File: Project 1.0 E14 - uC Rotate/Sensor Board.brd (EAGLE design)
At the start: 40 x 75 mm, 97 parts, among them IC1 LT1963EST-1.5, IC2 LT1963EST-1.5, IC3 LT1963EST-1.5, IC4 LT1963EST-1.5, X1 87438-02, X3 87438-04

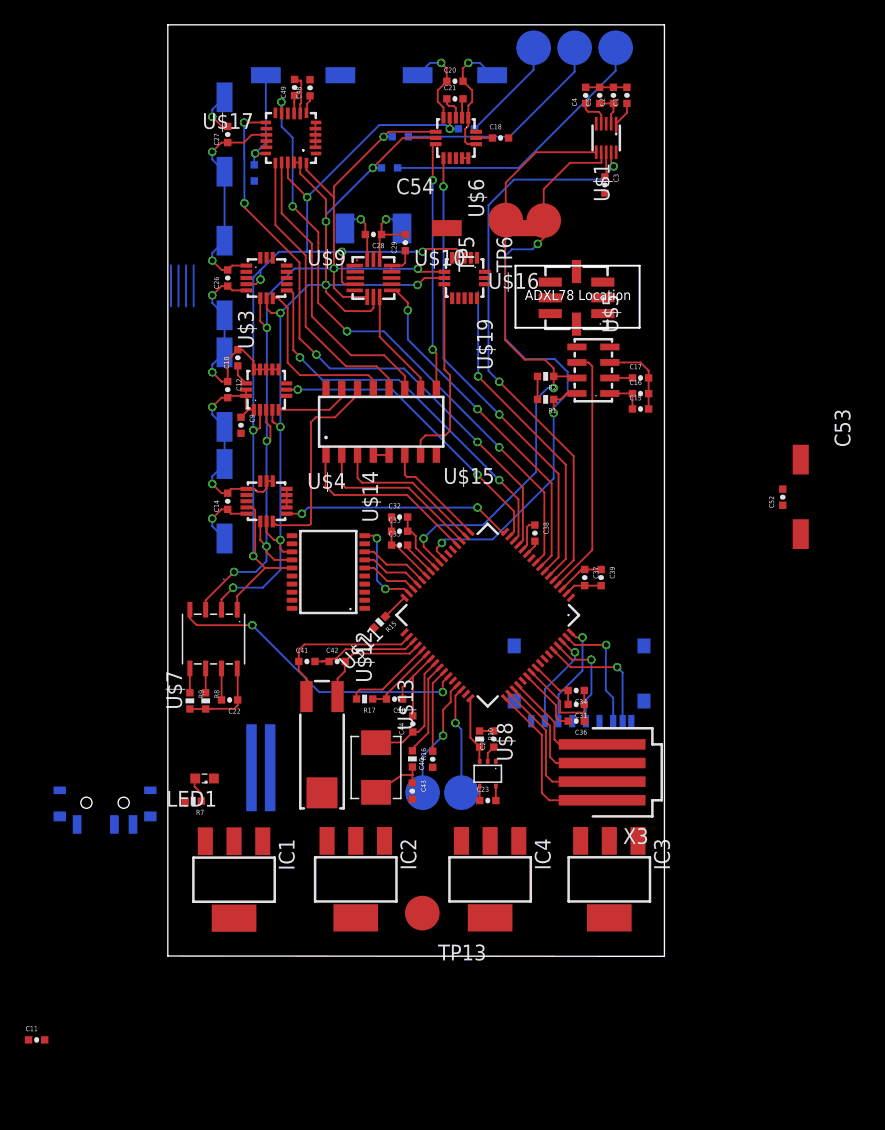
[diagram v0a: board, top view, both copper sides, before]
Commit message: Added H3LIS331 to library, Added H3LIS331 to schematic and removed ADXL78
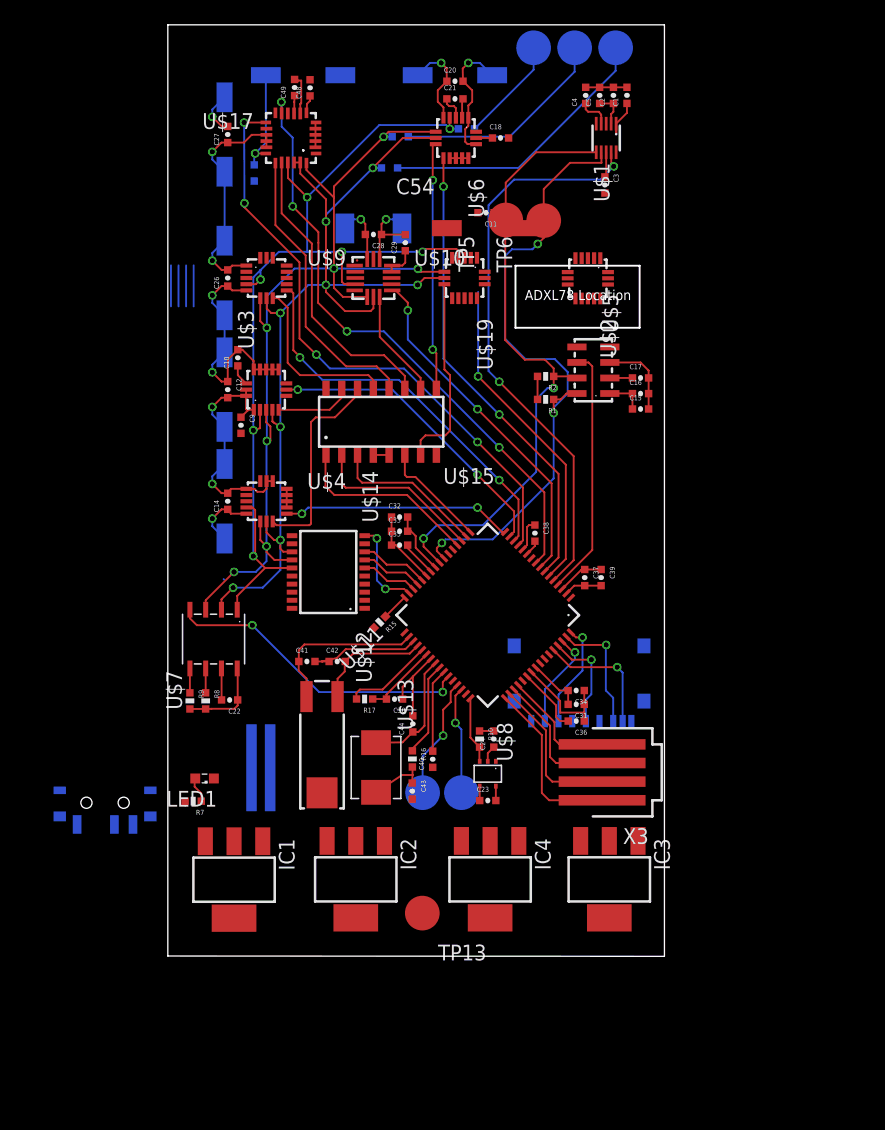
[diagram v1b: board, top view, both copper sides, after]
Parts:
- removed C52: 0.1uF, Kas-Passives:0402-CAP
- removed C53: 4.7uF, Kas-Passives:4.3X7.3SMD
- removed U$16: ADXL78, Kas-Sensors:LCC-8(5X5)_HS
- added U$2: H3LIS331DLTR_HS, Kas-Sensors:LGA-16(3X3)_HS
- moved C11 75.8 mm to (25.6, 59.9), turned to 180 degrees
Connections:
- removed net ADXL78-ST: U$16.P$4
- new net CS-H3LIS331DLTR: U$2.P$8
- new net N$37: U$2.P$1
- new net N$38: U$2.P$16
- new net N$39: U$2.P$14
- net 5.0V: no longer C52.1, C53.P$1, U$16.P$7, U$16.P$8
- net ANALOG-OUT-ADXL78: no longer U$16.P$6
- net GND: now also U$2.P$12, U$2.P$13, U$2.P$5; no longer C52.2, C53.P$2, U$16.P$3
- net MISO-B: now also U$2.P$7
- net MOSI-B: now also U$2.P$6
- net SCLK-B: now also U$2.P$4
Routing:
- net GND: track 92.5 -> 93.5 mm

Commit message: Sensor Board: Changed connector footprints to the correct model. Removed ADXL78 and replaced with H3LIS331DLTR.
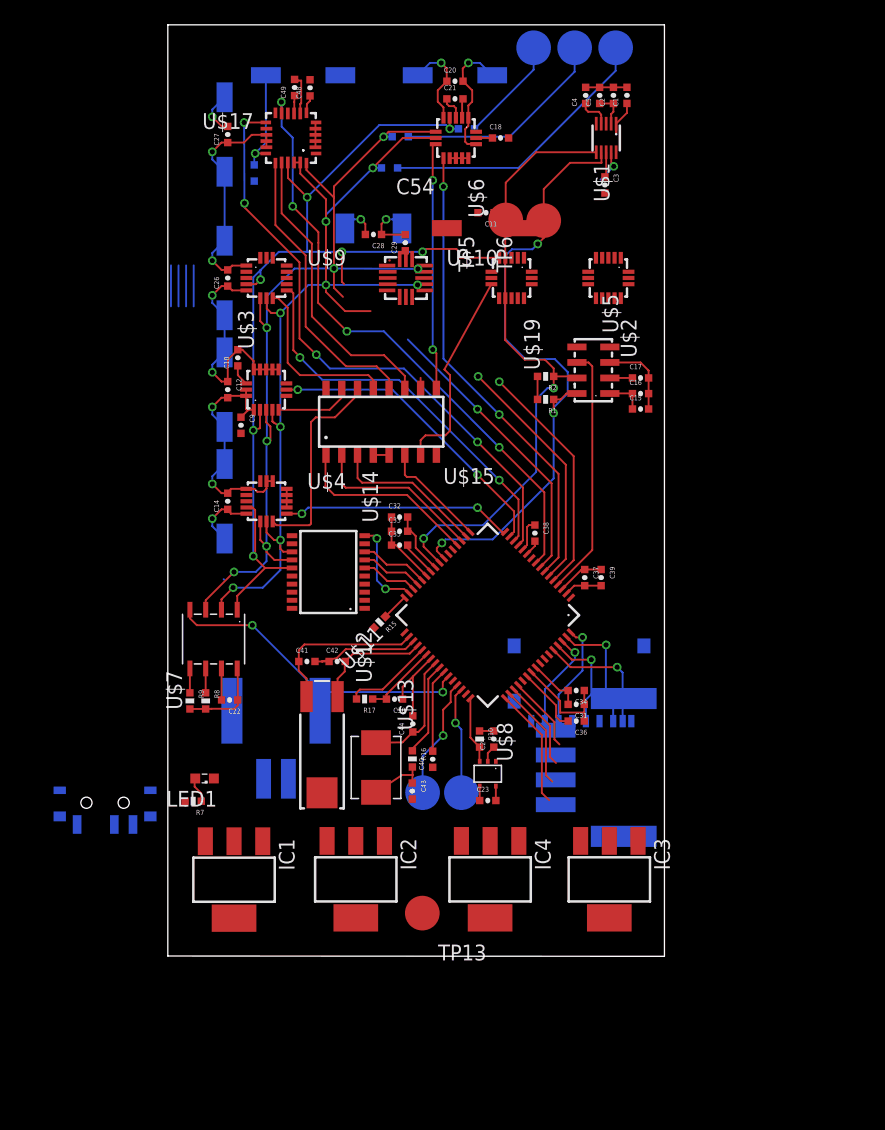
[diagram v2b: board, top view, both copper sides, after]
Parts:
- removed X1: 87438-02, con-molex:87438-02
- removed X3: 87438-04, con-molex:87438-04
- added U$16: 5023520200, Kas-Connectors:5023520200
- added U$20: 5023520410, Kas-Connectors:5023520410
- moved U$19 3.78 mm to (27.7, 54.6)
- moved U$10 2.62 mm to (19.2, 54.6)
- moved U$2 1.65 mm to (35.5, 54.6)
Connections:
- net GND: now also U$16.P$1; no longer X1.1
- net N$19: now also U$16.P$2; no longer X1.2
- net SWCLK: now also U$20.P$1; no longer X3.4
- net SWDIO: now also U$20.P$2; no longer X3.3
- net SWO: now also U$20.P$4; no longer X3.1
- net TDI: now also U$20.P$3; no longer X3.2
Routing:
- net INT1-MAG3110: track 46.4 -> 22.0 mm
- net CS-ADXL362: track 8.75 -> 0.86 mm
- net INT2-MAX21000: track 26.3 -> 19.5 mm
- net MOSI-B: track 80.2 -> 75.5 mm
- net INT2-ADXL362: track 28.1 -> 23.5 mm, vias 2 -> 1
- net SWO: track 14.0 -> 9.68 mm
- net TDI: track 12.5 -> 8.49 mm
- net SWDIO: track 11.0 -> 7.33 mm
- net MISO-B: track 79.3 -> 75.7 mm
- net GND: track 93.5 -> 90.0 mm
- net SWCLK: track 9.58 -> 6.15 mm
- net SCLK-B: track 84.1 -> 87.0 mm
- net 3.3V: track 96.7 -> 94.9 mm
- net CS-MAX21000: track 15.9 -> 16.8 mm
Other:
- outline, holes or cut-outs redrawn
- board text removed: "ADXL78 Location"
- board text removed: "FIX Footprint"
- board text removed: "H3LIS331DLTR should be used instead of teh ADXL78"

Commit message: Sensor Board: Removed all errors in PCB layout and most errors in schematic view. This was mainly achived by removing traces on the PCB and adding node names on the schematic
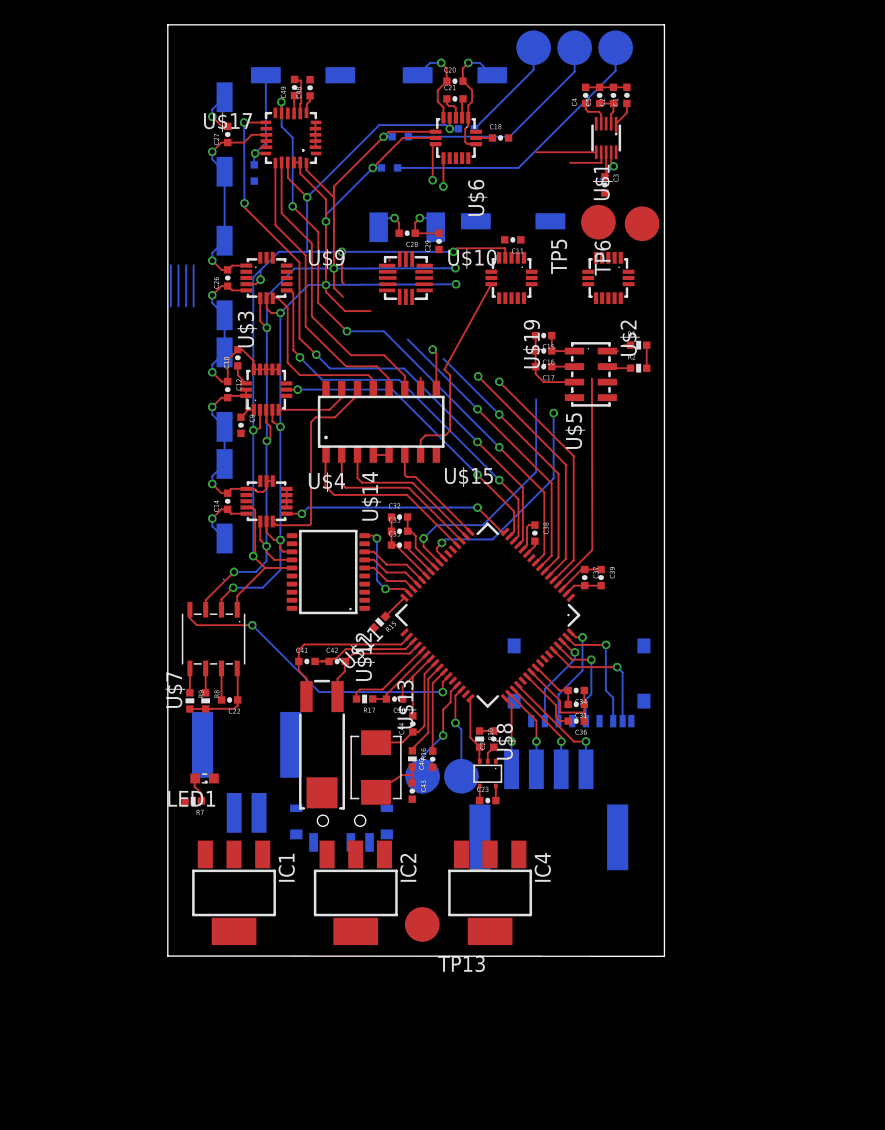
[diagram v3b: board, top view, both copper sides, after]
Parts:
- removed IC3: LT1963EST-1.5, linear-technology:SOT223
- C11: value CAPACITOR -> NO VALUE
- C54: value (none) -> NO VALUE
- U$19: value (none) -> MAX21000_HS
- moved S1 19.1 mm to (14.0, 10.9)
- moved U$20 12.0 mm to (30.7, 6.91), turned to 0 degrees
- moved C15 9.79 mm to (30.3, 50.0), turned to 180 degrees
- moved R1 8.67 mm to (37.9, 49.2), turned to 0 degrees
- moved C16 8.52 mm to (30.3, 48.7), turned to 180 degrees
- moved TP6 7.93 mm to (38.2, 59.0)
- moved C17 7.85 mm to (30.3, 47.5), turned to 180 degrees
- moved R2 7.52 mm to (37.9, 47.3), turned to 0 degrees
- moved TP5 7.47 mm to (34.7, 59.1)
- moved U$16 3.62 mm to (6.35, 19.7)
- moved C11 3.07 mm to (27.8, 57.7)
- moved C19 2.72 mm to (19.3, 58.7)
- moved C28 2.72 mm to (19.3, 58.2)
- moved C29 2.72 mm to (21.8, 57.6)
- moved C54 2.40 mm to (27.8, 59.2), flipped to the bottom, turned to 0 degrees
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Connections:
- removed net 5.0V: IC3.3
- removed net ANALOG-OUT-ADXL78: U$11.P$1
- removed net INT1-ADXL362: U$10.P$11
- removed net N$37: U$2.P$1
- removed net N$38: U$2.P$16
- removed net N$39: U$2.P$14
- net 3.0V: now also U$2.P$1
- net 3.3V: now also U$2.P$14
- net CS-H3LIS331DLTR: now also U$11.P$10
- net GND: now also U$2.P$16; no longer IC3.2, IC3.4
- net N$23: no longer IC3.1
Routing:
- net SCL-0: track 51.9 -> 22.9 mm, vias 3 -> 2
- net SDA-0: track 51.2 -> 26.3 mm, vias 2 -> 1
- net INT2-LSM303: track 37.6 -> 23.7 mm
- net CS-LSM303: track 20.3 -> 6.65 mm
- net SWCLK: track 6.15 -> 9.61 mm, vias 0 -> 1
- net SWO: track 9.68 -> 6.31 mm, vias 0 -> 1
- net MISO-B: track 75.7 -> 78.8 mm
- net MOSI-B: track 75.5 -> 78.5 mm
- net GND: track 90.0 -> 87.6 mm
- net INT1-MPL311: track 20.1 -> 17.8 mm
- net U1TX: track 8.70 -> 7.38 mm
- net TDI: track 8.49 -> 7.21 mm, vias 0 -> 1
- net SWDIO: track 7.33 -> 8.24 mm, vias 0 -> 1

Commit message: Sensor Board: Removed all errors in PCB layout and most errors in schematic view. This was mainly achived by removing traces on the PCB and adding node names o
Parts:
- added C6: 0.1uF, Kas-Passives:0402-CAP
- added C7: 10uF, Kas-Passives:4.3X7.3SMD
- added C8: 100nF, Kas-Passives:0402-CAP
- C11: value NO VALUE -> 1uF
- C54: value NO VALUE -> 10uF
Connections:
- net 3.3V: now also C6.1, C7.P$1, C8.1
- net GND: now also C6.2, C7.P$2, C8.2
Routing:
- net CS-MAX21000: track 16.8 -> 9.00 mm
- net SCLK-B: track 87.2 -> 82.9 mm, vias 7 -> 6
- net MOSI-B: vias 7 -> 6
- net MISO-B: vias 8 -> 7
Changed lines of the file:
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@@
 <element name="R6" library="Kas-Passives" package="0402-RES" value="0" x="17.8562" y="63.4746" rot="MR180"/>
 <element name="U$19" library="Kas-Sensors" package="LGA-16(3X3)_HS" value="MAX21000_HS" x="27.686" y="54.61" rot="R270"/>
-<element name="C11" library="Kas-Passives" package="0402-CAP" value="NO VALUE" x="27.7876" y="57.6834" rot="R180"/>
-<element name="C54" library="Kas-Passives" package="4.3X7.3SMD" value="NO VALUE" x="27.813" y="59.182" rot="MR0"/>
+<element name="C11" library="Kas-Passives" package="0402-CAP" value="1uF" x="27.7876" y="57.6834" rot="R180"/>
+<element name="C54" library="Kas-Passives" package="4.3X7.3SMD" value="10uF" x="27.813" y="59.182" rot="MR0"/>
 <element name="U$2" library="Kas-Sensors" package="LGA-16(3X3)_HS" value="H3LIS331DLTR_HS" x="35.4838" y="54.61" rot="R270"/>
 <element name="U$16" library="Kas-Connectors" package="5023520200" value="5023520200" x="6.35" y="19.6596" rot="MR180"/>
 <element name="U$20" library="Kas-Connectors" package="5023520410" value="5023520410" x="30.6832" y="6.9088" rot="MR0"/>
+<element name="C6" library="Kas-Passives" package="0402-CAP" value="0.1uF" x="-6.6294" y="-2.9718"/>
+<element name="C7" library="Kas-Passives" package="4.3X7.3SMD" value="10uF" x="-3.9624" y="-6.8834"/>
+<element name="C8" library="Kas-Passives" package="0402-CAP" value="100nF" x="-9.525" y="-11.7348"/>
 </elements>
 <signals>
@@
 <contactref element="U$16" pad="P$1"/>
 <contactref element="U$2" pad="P$16"/>
+<contactref element="C6" pad="2"/>
+<contactref element="C7" pad="P$2"/>
+<contactref element="C8" pad="2"/>
 <wire x1="34.5058" y1="67.0376" x2="34.7804" y2="69.9666" width="0" layer="19" extent="1-1"/>
 <wire x1="36.1058" y1="64.7376" x2="34.5058" y2="67.0376" width="0" layer="19" extent="1-1"/>
@@
 <wire x1="5.334" y1="1.981" x2="5.334" y2="8.1788" width="0" layer="19" extent="1-1"/>
 <wire x1="4.3284" y1="20.6248" x2="3.7091" y2="14.3002" width="0" layer="19" extent="1-1"/>
+<wire x1="-0.9624" y1="-6.8834" x2="5.334" y2="1.981" width="0" layer="19" extent="1-1"/>
+<wire x1="-5.9794" y1="-2.9718" x2="-0.9624" y2="-6.8834" width="0" layer="19" extent="1-1"/>
+<wire x1="-8.875" y1="-11.7348" x2="-5.9794" y2="-2.9718" width="0" layer="19" extent="1-1"/>
 </signal>
 <signal name="N$1">
@@
 <wire x1="7.4422" y1="52.88175" x2="7.4422" y2="51.1336" width="0.1524" layer="1"/>
 <wire x1="13.37945" y1="55.372" x2="10.2108" y2="55.372" width="0.1524" layer="16"/>
-<via x="23.1648" y="55.3974" extent="1-16" drill="0.4064"/>
 <wire x1="10.0036" y1="31.90355" x2="8.58405" y2="31.90355" width="0.1524" layer="1"/>
 <wire x1="5.334" y1="30.9372" x2="7.0866" y2="30.9372" width="0.1524" layer="16"/>
@@
 <contactref element="U$2" pad="P$6"/>
 <wire x1="26.061" y1="55.11" x2="33.8588" y2="55.11" width="0" layer="19" extent="1-1"/>
-<wire x1="23.1648" y1="55.3974" x2="26.061" y2="55.11" width="0" layer="19" extent="1-1"/>
+<wire x1="23.1648" y1="55.3974" x2="26.061" y2="55.11" width="0" layer="19" extent="1-16"/>
 <wire x1="18.677" y1="53.085" x2="14.1097" y2="53.086" width="0" layer="19" extent="1-1"/>
 </signal>
@@
 <wire x1="12.7381" y1="59.1566" x2="12.7381" y2="54.0512" width="0.1524" layer="1"/>
 <wire x1="10.166159375" y1="63.9126" x2="10.666159375" y2="63.9126" width="0.1524" layer="1"/>
-<via x="23.2156" y="54.102" extent="1-16" drill="0.4064"/>
 <wire x1="14.2748" y1="51.943" x2="16.3322" y2="51.943" width="0.1524" layer="1"/>
 <wire x1="9.0678" y1="51.7906" x2="11.3284" y2="54.0512" width="0.1524" layer="16"/>
@@
 <contactref element="U$2" pad="P$7"/>
 <wire x1="26.061" y1="54.61" x2="33.8588" y2="54.61" width="0" layer="19" extent="1-1"/>
-<wire x1="23.2156" y1="54.102" x2="26.061" y2="54.61" width="0" layer="19" extent="1-1"/>
+<wire x1="23.2156" y1="54.102" x2="26.061" y2="54.61" width="0" layer="19" extent="1-16"/>
 <wire x1="19.177" y1="53.085" x2="16.3322" y2="51.943" width="0" layer="19" extent="1-1"/>
 </signal>
@@
 <contactref element="C54" pad="P$1"/>
 <contactref element="U$2" pad="P$14"/>
+<contactref element="C6" pad="1"/>
+<contactref element="C8" pad="1"/>
+<contactref element="C7" pad="P$1"/>
 <wire x1="35.3058" y1="64.7376" x2="35.7058" y2="67.0376" width="0" layer="19" extent="1-1"/>
 <wire x1="30.813" y1="59.182" x2="35.2044" y2="62.753" width="0" layer="19" extent="1-16"/>
@@
 <wire x1="1.3947" y1="12.4714" x2="1.778" y2="19.8986" width="0" layer="19" extent="1-1"/>
 <wire x1="12.827" y1="8.1788" x2="21.336" y2="16.4996" width="0" layer="19" extent="1-1"/>
+<wire x1="-7.2794" y1="-2.9718" x2="1.397" y2="12.0904" width="0" layer="19" extent="1-1"/>
+<wire x1="-6.9624" y1="-6.8834" x2="-7.2794" y2="-2.9718" width="0" layer="19" extent="1-1"/>
+<wire x1="-10.175" y1="-11.7348" x2="-6.9624" y2="-6.8834" width="0" layer="19" extent="1-1"/>
 </signal>
 <signal name="N$23">
@@
 <wire x1="9.6774" y1="63.901359375" x2="9.6774" y2="62.6618" width="0.1524" layer="1"/>
 <wire x1="11.22360625" y1="61.11559375" x2="11.22360625" y2="56.7182" width="0.1524" layer="16"/>
-<via x="23.0124" y="56.7182" extent="1-16" drill="0.4064"/>
 <wire x1="14.0208" y1="56.7182" x2="14.0208" y2="54.3052" width="0.1524" layer="1"/>
 <wire x1="14.0208" y1="54.3052" x2="14.1986" y2="54.1274" width="0.1524" layer="1"/>
@@
 <wire x1="23.4038" y1="66.6242" x2="22.7076" y2="66.6242" width="0.1524" layer="16"/>
 <contactref element="U$19" pad="P$4"/>
-<wire x1="23.0378" y1="56.7182" x2="23.3172" y2="56.9976" width="0.1524" layer="1"/>
-<wire x1="23.3172" y1="56.9976" x2="27.178" y2="57.005" width="0.1524" layer="1"/>
 <wire x1="27.178" y1="57.005" x2="27.186" y2="56.235" width="0.1524" layer="1"/>
 <contactref element="U$2" pad="P$4"/>
 <wire x1="27.186" y1="56.235" x2="34.9838" y2="56.235" width="0" layer="19" extent="1-1"/>
-<wire x1="23.0124" y1="56.7182" x2="23.0378" y2="56.7182" width="0" layer="19" extent="1-1"/>
+<wire x1="23.0124" y1="56.7182" x2="27.178" y2="57.005" width="0" layer="19" extent="1-16"/>
 <wire x1="17.7145" y1="54.11" x2="14.1986" y2="54.1274" width="0" layer="19" extent="1-1"/>
 </signal>
@@
 <wire x1="22.352" y1="41.9354" x2="22.733" y2="42.3164" width="0.1524" layer="1"/>
 <wire x1="22.733" y1="42.3164" x2="22.733" y2="46.7868" width="0.1524" layer="1"/>
-<wire x1="26.061" y1="54.11" x2="22.2764" y2="47.2434" width="0.1524" layer="1"/>
 <wire x1="22.2764" y1="47.2434" x2="22.733" y2="46.7868" width="0.1524" layer="1"/>
+<wire x1="22.2764" y1="47.2434" x2="26.061" y2="54.11" width="0" layer="19" extent="1-1"/>
 </signal>
 <signal name="INT2-MAX21000">
